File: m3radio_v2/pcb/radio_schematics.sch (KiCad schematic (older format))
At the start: 21 parts, among them IC201 Si4460, P201 COAX, Y201 TCXO

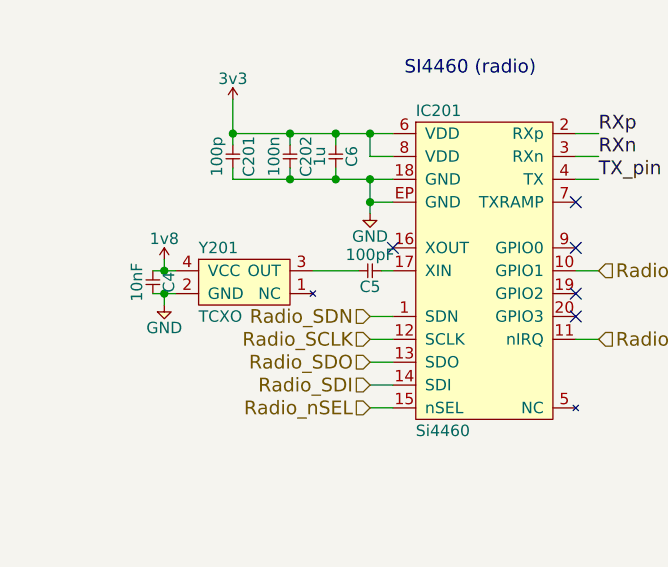
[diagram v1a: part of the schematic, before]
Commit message: Merge with master again and add SL18860DC
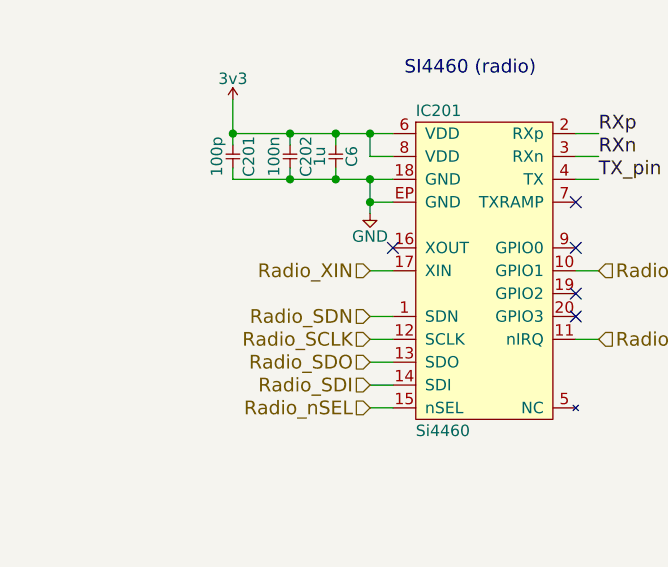
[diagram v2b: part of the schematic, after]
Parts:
- removed C4: 10nF, agg:0402, symbol C
- removed C5: 100pF, agg:0402, symbol C
- removed Y201: TCXO, agg:TG-5006CG, symbol TCXO
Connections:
- net Radio_XIN: now reaches IC201.17 (XIN)
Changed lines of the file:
@@
 Wire Wire Line
 	8350 4300 8350 4500
-$Comp
-L TCXO Y201
-U 1 1 56C5879C
-P 1500 2900
-F 0 "Y201" H 1300 3000 50  0000 L CNN
-F 1 "TCXO" H 1300 2700 50  0000 L CNN
-F 2 "agg:TG-5006CG" H 1300 2900 50  0001 C CNN
-F 3 "http://www.farnell.com/datasheets/1804153.pdf" H 1300 2900 50  0001 C CNN
-F 4 "2405785" H 1300 2600 50  0001 L CNN "Farnell"
-	1    1500 2900
-	1    0    0    -1
-$EndComp
-Wire Wire Line
-	1100 2900 1200 2900
-Wire Wire Line
-	1100 3000 1200 3000
-Wire Wire Line
-	1150 3000 1150 3050
-$Comp
-L GND #PWR050
-U 1 1 56C60D0D
-P 1150 3050
-F 0 "#PWR050" H 1020 3090 50  0001 L CNN
-F 1 "GND" H 1150 2950 50  0000 C CNN
-F 2 "" H 1150 3050 60  0000 C CNN
-F 3 "" H 1150 3050 60  0000 C CNN
-	1    1150 3050
-	1    0    0    -1
-$EndComp
 NoConn ~ 2150 2800
 $Comp
@@
 	8200 4250 8200 4200
 Connection ~ 8200 4200
-$Comp
-L C C4
-U 1 1 576B8629
-P 1100 2900
-F 0 "C4" H 1150 2970 50  0000 C CNN
-F 1 "10nF" H 1150 2830 50  0000 C CNN
-F 2 "agg:0402" H 1100 2900 50  0001 C CNN
-F 3 "" H 1100 2900 50  0001 C CNN
-F 4 "1414575" H 1100 2900 60  0001 C CNN "Farnell"
-	1    1100 2900
-	0    1    1    0
-$EndComp
-Connection ~ 1150 2900
-Connection ~ 1150 3000
-$Comp
-L C C5
-U 1 1 576B8ADE
-P 2100 2900
-F 0 "C5" H 2150 2970 50  0000 C CNN
-F 1 "100pF" H 2150 2830 50  0000 C CNN
-F 2 "agg:0402" H 2100 2900 50  0001 C CNN
-F 3 "" H 2100 2900 50  0001 C CNN
-F 4 "2496792" H 2100 2900 60  0001 C CNN "Farnell"
-	1    2100 2900
-	-1   0    0    1
-$EndComp
 Wire Wire Line
-	1800 2900 2000 2900
-Wire Wire Line
-	2100 2900 2150 2900
+	2050 2900 2150 2900
 Text HLabel 3050 2900 2    60   Input ~ 0
 Radio_GPIO1
@@
 Wire Wire Line
 	2150 3100 2050 3100
-$Comp
-L 1v8 #PWR052
-U 1 1 576ED3BF
-P 1150 2850
-F 0 "#PWR052" H 1150 2960 50  0001 L CNN
-F 1 "1v8" H 1150 2940 50  0000 C CNN
-F 2 "" H 1150 2850 60  0000 C CNN
-F 3 "" H 1150 2850 60  0000 C CNN
-	1    1150 2850
-	1    0    0    -1
-$EndComp
-Wire Wire Line
-	1150 2900 1150 2850
+Text HLabel 2050 2900 0    60   Input ~ 0
+Radio_XIN
 $EndSCHEMATC

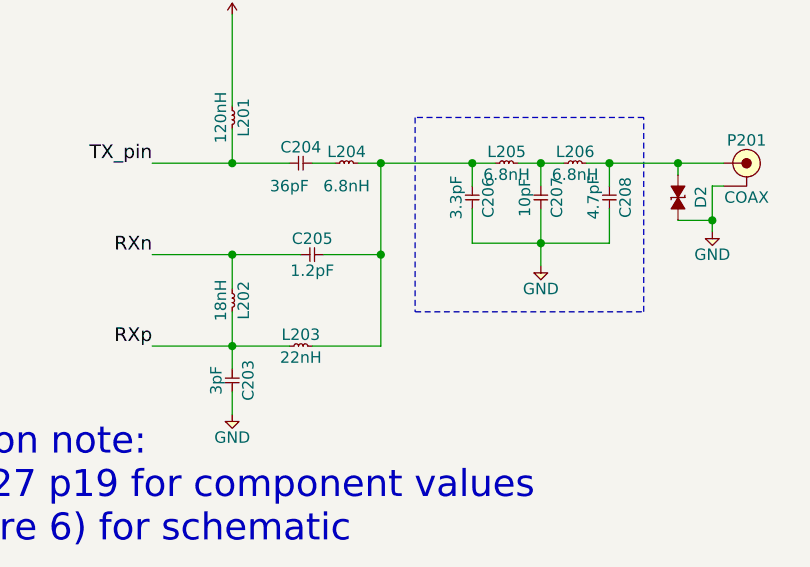
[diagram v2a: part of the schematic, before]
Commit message: Finish schematic, begin routing
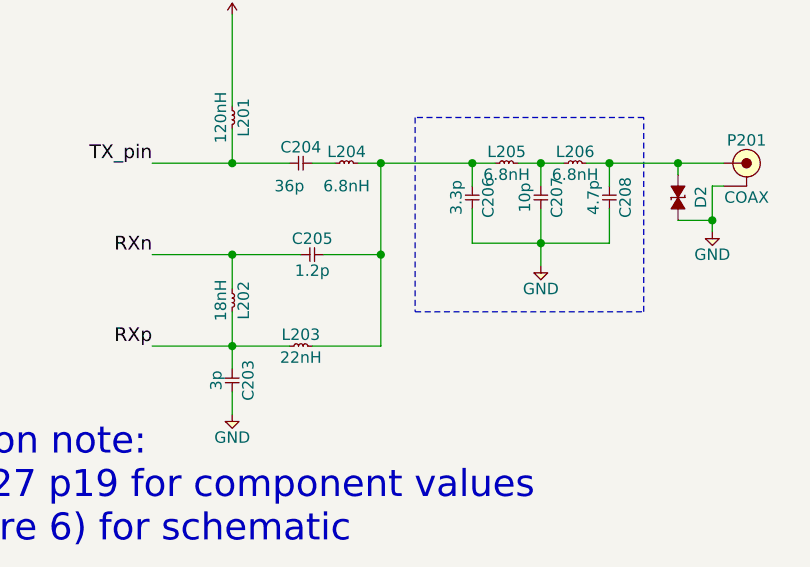
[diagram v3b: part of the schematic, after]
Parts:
- C203: value 3pF -> 3p
- C204: value 36pF -> 36p
- C205: value 1.2pF -> 1.2p
- C206: value 3.3pF -> 3.3p
- C207: value 10pF -> 10p
- C208: value 4.7pF -> 4.7p
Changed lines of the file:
@@
 Radio_nSEL
 $Comp
-L GND #PWR045
+L GND #PWR059
 U 1 1 56B22850
 P 2050 2650
-F 0 "#PWR045" H 1920 2690 50  0001 L CNN
+F 0 "#PWR059" H 1920 2690 50  0001 L CNN
 F 1 "GND" H 2050 2550 50  0000 C CNN
 F 2 "" H 2050 2650 60  0000 C CNN
@@
 $EndComp
 $Comp
-L 3v3 #PWR046
+L 3v3 #PWR060
 U 1 1 56B228AE
 P 1450 2150
-F 0 "#PWR046" H 1450 2260 50  0001 L CNN
+F 0 "#PWR060" H 1450 2260 50  0001 L CNN
 F 1 "3v3" H 1450 2240 50  0000 C CNN
 F 2 "" H 1450 2150 60  0000 C CNN
@@
 P 6500 4200
 F 0 "C204" H 6550 4270 50  0000 C CNN
-F 1 "36pF" H 6500 4100 50  0000 C CNN
+F 1 "36p" H 6500 4100 50  0000 C CNN
 F 2 "agg:0402" H 6500 4200 50  0001 C CNN
 F 3 "" H 6500 4200 50  0001 C CNN
@@
 P 6550 4600
 F 0 "C205" H 6600 4670 50  0000 C CNN
-F 1 "1.2pF" H 6600 4530 50  0000 C CNN
+F 1 "1.2p" H 6600 4530 50  0000 C CNN
 F 2 "agg:0402" H 6550 4600 50  0001 C CNN
 F 3 "" H 6550 4600 50  0001 C CNN
@@
 P 6250 5100
 F 0 "C203" H 6300 5170 50  0000 C CNN
-F 1 "3pF" H 6300 5030 50  0000 C CNN
+F 1 "3p" H 6300 5030 50  0000 C CNN
 F 2 "agg:0402" H 6250 5100 50  0001 C CNN
 F 3 "" H 6250 5100 50  0001 C CNN
@@
 $EndComp
 $Comp
-L GND #PWR047
+L GND #PWR061
 U 1 1 56B2404E
 P 6250 5300
-F 0 "#PWR047" H 6120 5340 50  0001 L CNN
+F 0 "#PWR061" H 6120 5340 50  0001 L CNN
 F 1 "GND" H 6250 5200 50  0000 C CNN
 F 2 "" H 6250 5300 60  0000 C CNN
@@
 P 7300 4300
 F 0 "C206" H 7350 4370 50  0000 C CNN
-F 1 "3.3pF" H 7350 4230 50  0000 C CNN
+F 1 "3.3p" H 7350 4230 50  0000 C CNN
 F 2 "agg:0402" H 7300 4300 50  0001 C CNN
 F 3 "" H 7300 4300 50  0001 C CNN
@@
 P 7600 4300
 F 0 "C207" H 7650 4370 50  0000 C CNN
-F 1 "10pF" H 7650 4230 50  0000 C CNN
+F 1 "10p" H 7650 4230 50  0000 C CNN
 F 2 "agg:0402" H 7600 4300 50  0001 C CNN
 F 3 "" H 7600 4300 50  0001 C CNN
@@
 P 7900 4300
 F 0 "C208" H 7950 4370 50  0000 C CNN
-F 1 "4.7pF" H 7950 4230 50  0000 C CNN
+F 1 "4.7p" H 7950 4230 50  0000 C CNN
 F 2 "agg:0402" H 7900 4300 50  0001 C CNN
 F 3 "" H 7900 4300 50  0001 C CNN
@@
 $EndComp
 $Comp
-L GND #PWR048
+L GND #PWR062
 U 1 1 56B24884
 P 7600 4650
-F 0 "#PWR048" H 7470 4690 50  0001 L CNN
+F 0 "#PWR062" H 7470 4690 50  0001 L CNN
 F 1 "GND" H 7600 4550 50  0000 C CNN
 F 2 "" H 7600 4650 60  0000 C CNN
@@
 $EndComp
 $Comp
-L GND #PWR049
+L GND #PWR063
 U 1 1 56B30843
 P 8350 4500
-F 0 "#PWR049" H 8220 4540 50  0001 L CNN
+F 0 "#PWR063" H 8220 4540 50  0001 L CNN
 F 1 "GND" H 8350 4400 50  0000 C CNN
 F 2 "" H 8350 4500 60  0000 C CNN
@@
 NoConn ~ 2150 2800
 $Comp
-L 3v3 #PWR051
+L 3v3 #PWR064
 U 1 1 576AEE23
 P 6250 3550
-F 0 "#PWR051" H 6250 3660 50  0001 L CNN
+F 0 "#PWR064" H 6250 3660 50  0001 L CNN
 F 1 "3v3" H 6250 3640 50  0000 C CNN
 F 2 "" H 6250 3550 60  0000 C CNN
